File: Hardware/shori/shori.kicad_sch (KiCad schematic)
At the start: 107 parts, among them J1 430450200, J2 SWD_Header, J3 UART_Header, J4 530480310, J5 Conn_01x03, J6 530480210, J7 530480210, SW1 SW_SPDT, SW2 SW_Push, U1 CS4272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

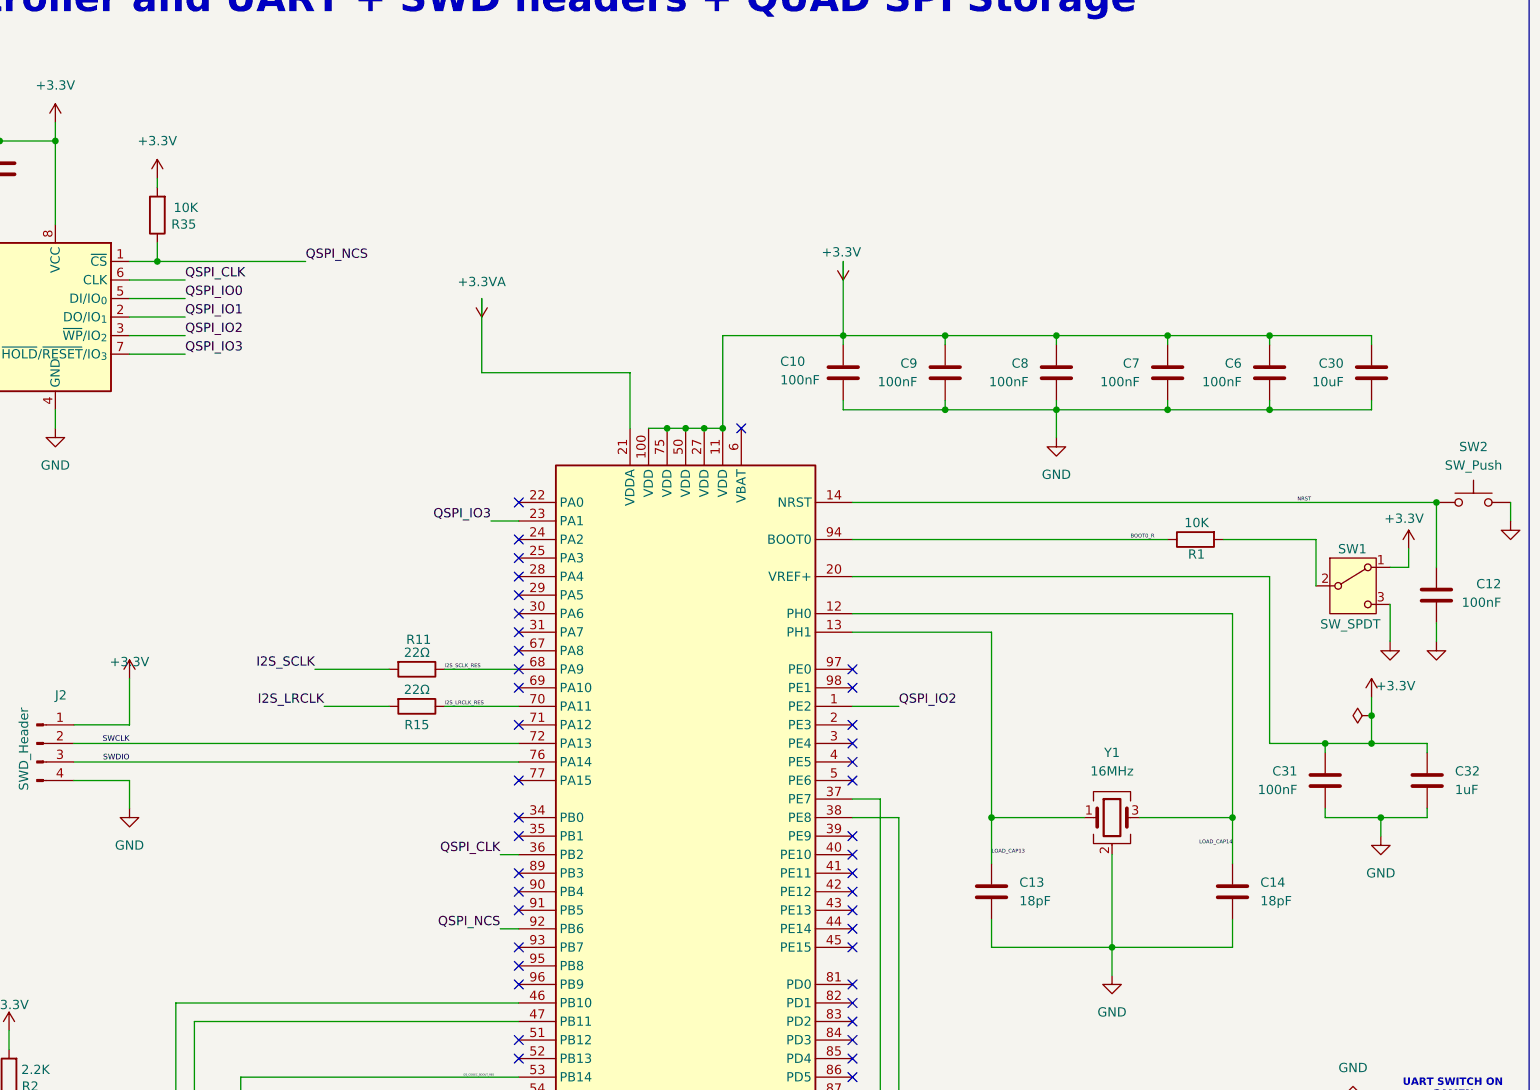
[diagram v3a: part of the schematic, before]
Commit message: Flash, boot0 switch, led, and nrst button routed. The board is done!
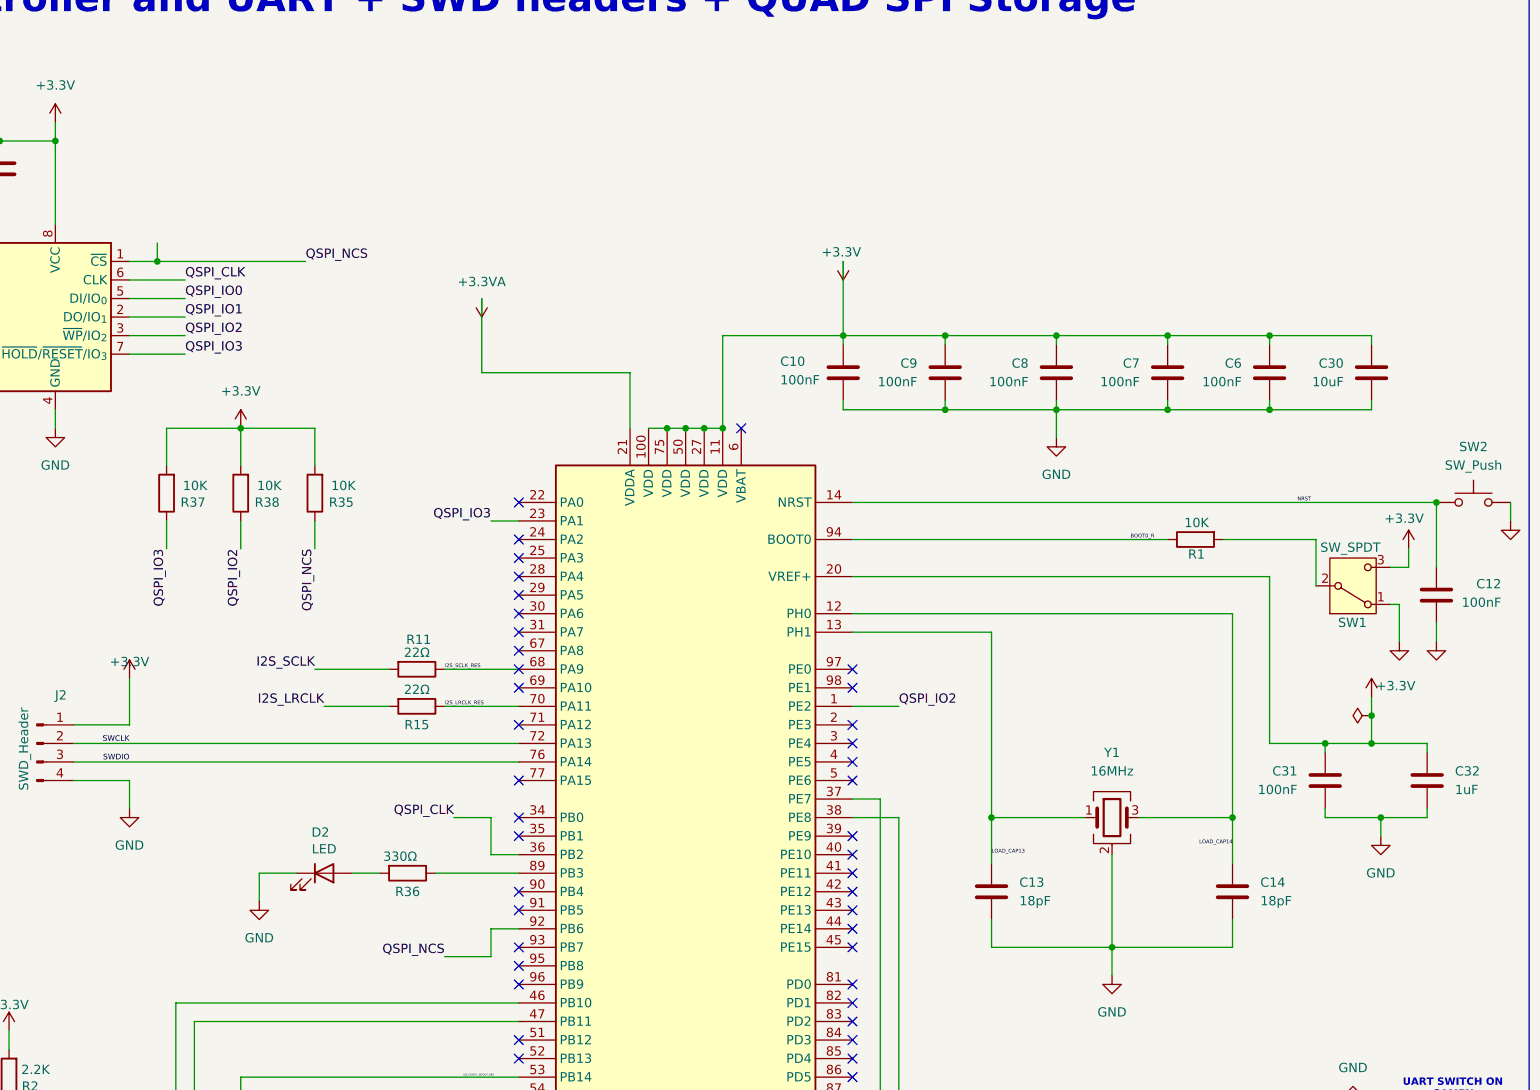
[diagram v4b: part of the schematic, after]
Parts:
- added D2: LED, LED_SMD:LED_0402_1005Metric_Pad0.77x0.64mm_HandSolder, symbol Device:LED
- added R36: 330Ω, Resistor_SMD:R_0402_1005Metric_Pad0.72x0.64mm_HandSolder, symbol Device:R
- added R37, R38: 10K, Resistor_SMD:R_0402_1005Metric_Pad0.72x0.64mm_HandSolder, symbol Device:R
- C47: footprint Capacitor_SMD:C_0603_1608Metric_Pad1.08x0.95mm_HandSolder -> Capacitor_SMD:C_0402_1005Metric_Pad0.74x0.62mm_HandSolder
- SW1: footprint (none) -> Button_Switch_SMD:SW_SPDT_Shouhan_MSK12C02
- SW2: footprint (none) -> Button_Switch_SMD:SW_SPST_B3U-1000P
- Y1: footprint Crystal:Crystal_SMD_3225-4Pin_3.2x2.5mm_HandSoldering -> MyFootprints:XTAL_ABM8-12.288MHZ-B2-T
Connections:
- net +3.3V: now also SW1.3 (C), R37.2, R38.2; no longer SW1.1 (A)
- net GND: now also SW1.1 (A), D2.1 (K); no longer SW1.3 (C)
- net QSPI_IO2: now also R38.1
- net QSPI_IO3: now also R37.1
- net at U2.89 (PB3): now also R36.1
- new net: D2.2 (A), R36.2
- no-connect marks 70 -> 69
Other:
- moved on the sheet: R35

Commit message: Rev 3 changes: RC filters, Ideal diodes, electrical fixes, and their layout
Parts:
- removed C15: 10μF, Capacitor_SMD:C_0603_1608Metric_Pad1.08x0.95mm_HandSolder, symbol Device:C
- removed C16: 100nF, Capacitor_SMD:C_0402_1005Metric_Pad0.74x0.62mm_HandSolder, symbol Device:C
- removed D1: D_Schottky, Diode_SMD:D_SOD-123, symbol Device:D_Schottky
- removed FB1, FB2: FerriteBead, Inductor_SMD:L_0805_2012Metric, symbol Device:FerriteBead
- added C15: 100uF, MyFootprints:CAPPM3216X180N, symbol TanCap:F930J107MAA
- added C49: 100nF, Capacitor_SMD:C_0402_1005Metric_Pad0.74x0.62mm_HandSolder, symbol Device:C
- added R39, R40: 10Ω, Resistor_SMD:R_0402_1005Metric_Pad0.72x0.64mm_HandSolder, symbol Device:R
- added U8: MAX40200AUK, Package_TO_SOT_SMD:SOT-23-5, symbol Analog_Switch:MAX40200AUK
- C1: value 4.7uf -> 100nF
- C4: value 100nF -> 10uF
- renumbered SW2 to RST1
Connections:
- net +3.3V: now also C1.1, R39.2
- net +3.3VA: now also R39.1; no longer C1.1
- net +5V: now also U8.1 (VDD), U8.3 (EN)
- net +5VA: now also C15.1, R40.1
- net GND: now also C15.2, C49.2, U8.2 (GND)
- net SWCLK: now also J2.3 (Pin_3), U2.76 (PA14); no longer J2.2 (Pin_2), U2.72 (PA13)
- net SWDIO: now also J2.2 (Pin_2), U2.72 (PA13); no longer J2.3 (Pin_3), U2.76 (PA14)
- net 5V_PROTECTED: now reaches C3.1, U5.1 (IN), U5.5 (EN)
- net 5V_PROTECTED: now also C49.1, R40.2, U8.5 (OUT)
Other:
- note added: "WAVEFORGE: SHORI REV 3"
- note removed: "WAVEFORGE: SHORI REV 2"
- moved on the sheet: C1, C3, C4, C5, U5

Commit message: Power LED added on schems
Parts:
- added D1: LED, LED_SMD:LED_0603_1608Metric_Pad1.05x0.95mm_HandSolder, symbol Device:LED
- added R41: 330Ω, Resistor_SMD:R_0402_1005Metric_Pad0.72x0.64mm_HandSolder, symbol Device:R
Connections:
- net +3.3V: now also R41.2
- net GND: now also D1.1 (K)
- net BOOT0_R_TO_SW: now reaches R1.2, SW1.2 (B)
- new net: D1.2 (A), R41.1
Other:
- note added: "Main Connectors: Power + AudioIn + AudioOut"
- note removed: "Shoyu Connectors: Power + AudioIn + AudioOut"
- moved on the sheet: C1, C3, C4, C5, R39, U5, U8

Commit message: Rev 3 main changes completed!
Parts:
- added D10, D11, D8, D9: BAT54C, Package_TO_SOT_SMD:SOT-23, symbol Diode:BAT54C
- added D7: PRTR5V0U2X, Package_TO_SOT_SMD:SOT-143, symbol Power_Protection:PRTR5V0U2X
- added R42, R43, R44, R45: 100Ω, Resistor_SMD:R_0402_1005Metric_Pad0.72x0.64mm_HandSolder, symbol Device:R
- added TP1: TP_5V, TestPoint:TestPoint_Pad_D1.0mm, symbol Connector:TestPoint
- added TP2: TP_3V3, TestPoint:TestPoint_Pad_D1.0mm, symbol Connector:TestPoint
- added TP3: TP_3V3A, TestPoint:TestPoint_Pad_D1.0mm, symbol Connector:TestPoint
- added TP4: TP_5VA, TestPoint:TestPoint_Pad_D1.0mm, symbol Connector:TestPoint
- added TP5: TP_MCLK, TestPoint:TestPoint_Pad_D1.0mm, symbol Connector:TestPoint
- added TP6: TP_UARTTX, TestPoint:TestPoint_Pad_D1.0mm, symbol Connector:TestPoint
- D1: footprint LED_SMD:LED_0603_1608Metric_Pad1.05x0.95mm_HandSolder -> LED_SMD:LED_0805_2012Metric_Pad1.15x1.40mm_HandSolder
- R41: value 330Ω -> 33Ω
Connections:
- net +3.3V: now also D7.4 (VCC), TP2.1; no longer C1.1
- net +3.3VA: now also C1.1, TP3.1
- net +5VA: now also C49.1, D10.2, D11.1, D8.2, D9.2, TP4.1
- net 5V_PROTECTED: now also TP1.1; no longer C49.1
- net AUDIO_IN+: now also R43.1
- net AUDIO_IN-: now also R42.2
- net GND: now also D10.1, D11.2, D7.1 (GND), D8.1, D9.1
- net I2S_MCLK: now also TP5.1
- net JACKR: now also R45.2
- net JACKT: now also R44.2
- net UART_RX_RES: now also D7.3 (I/O2)
- net UART_TX_RES: now also D7.2 (I/O1), TP6.1
- new net: D9.3, R42.1
- new net: D10.3, R44.1
- new net: D11.3, R45.1
- new net SHUNT_RES_AINP: D8.3, R43.2
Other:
- moved on the sheet: C1, C15, C33, C4, J1, J4, J6, J7, R10, R14, R39, R40

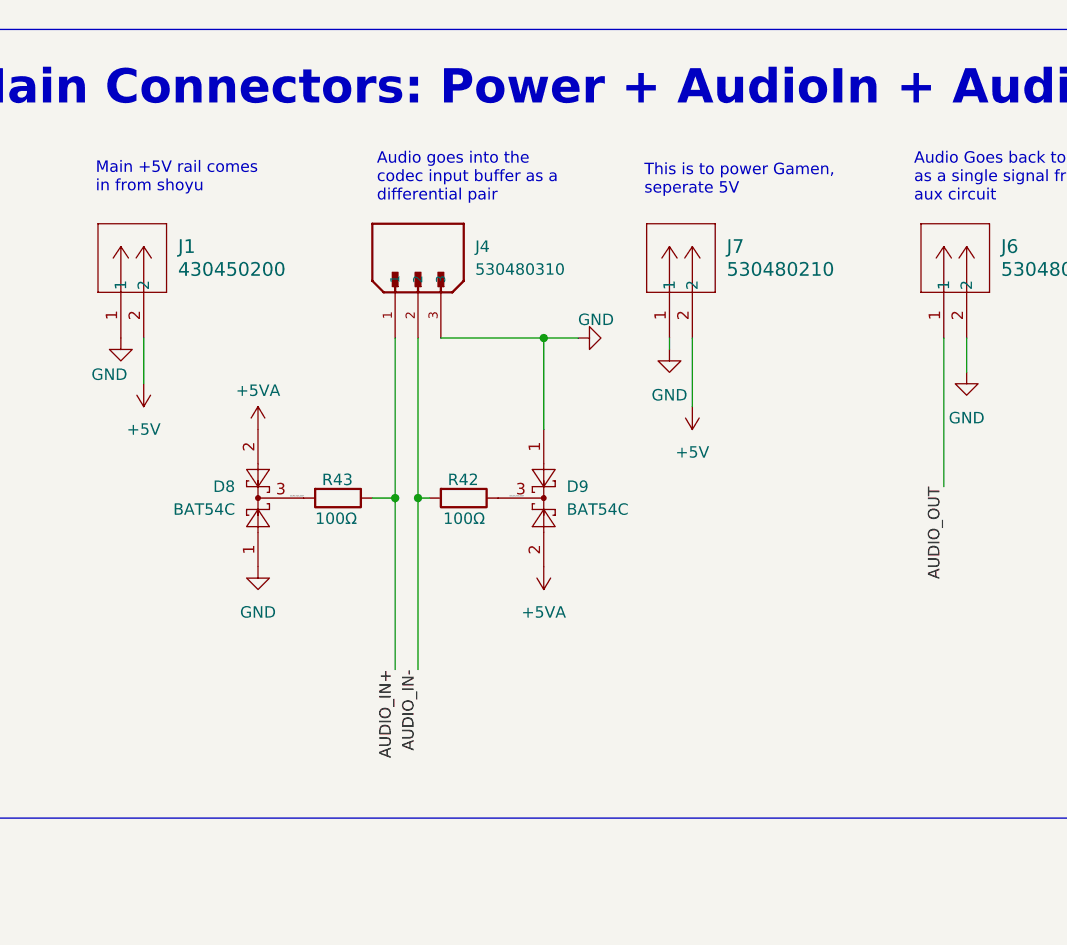
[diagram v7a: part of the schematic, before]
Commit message: removed gamen power conn and layout clean up
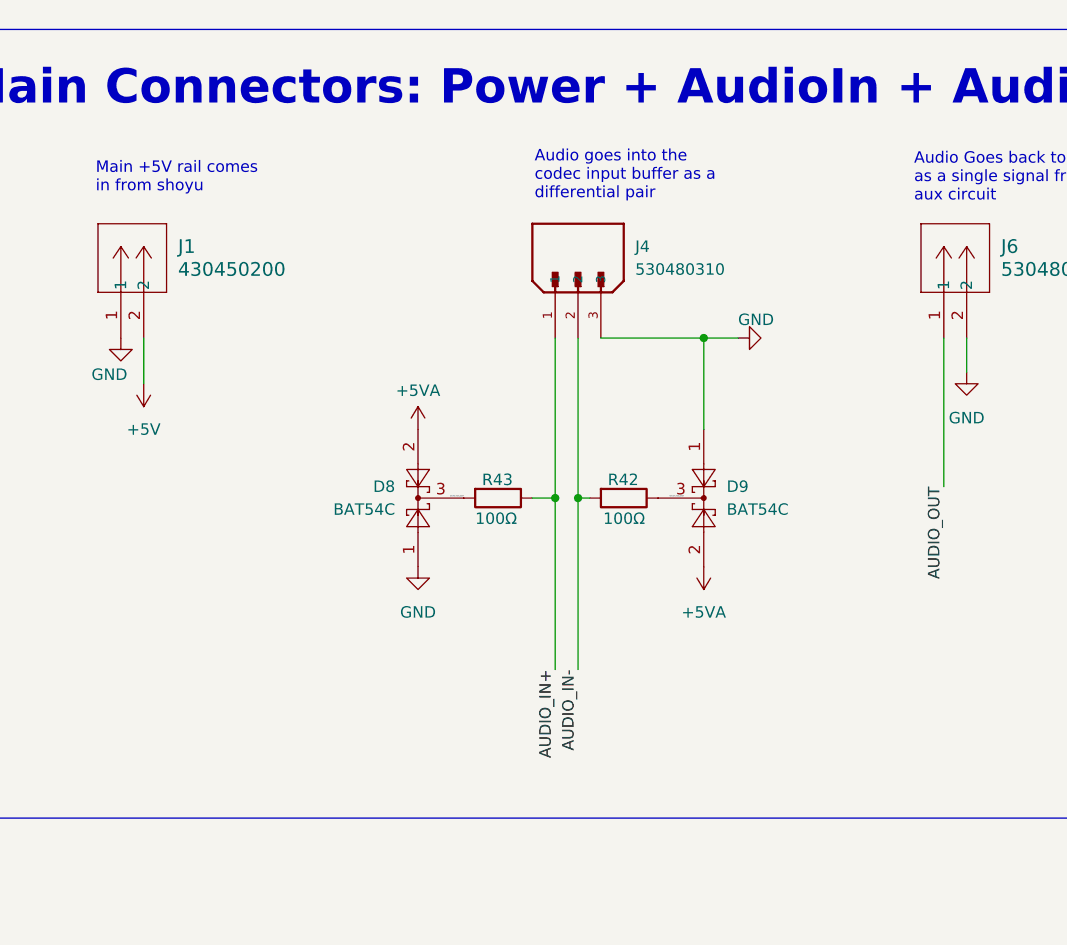
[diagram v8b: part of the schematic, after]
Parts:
- removed J7: 530480210, My footprints:CONN02_530480210_MOL, symbol 2 Pin Audio Molex:530480210
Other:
- note removed: "This is to power Gamen, seperate 5V"
- moved on the sheet: D8, D9, J4, R42, R43
